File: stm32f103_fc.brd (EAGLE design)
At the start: 37.7 x 72 mm, 50 parts, among them IC1 STM32F103C8T6, IC2 LD1117AS33TR, Y1 8MHz, Y2 32.768MHz

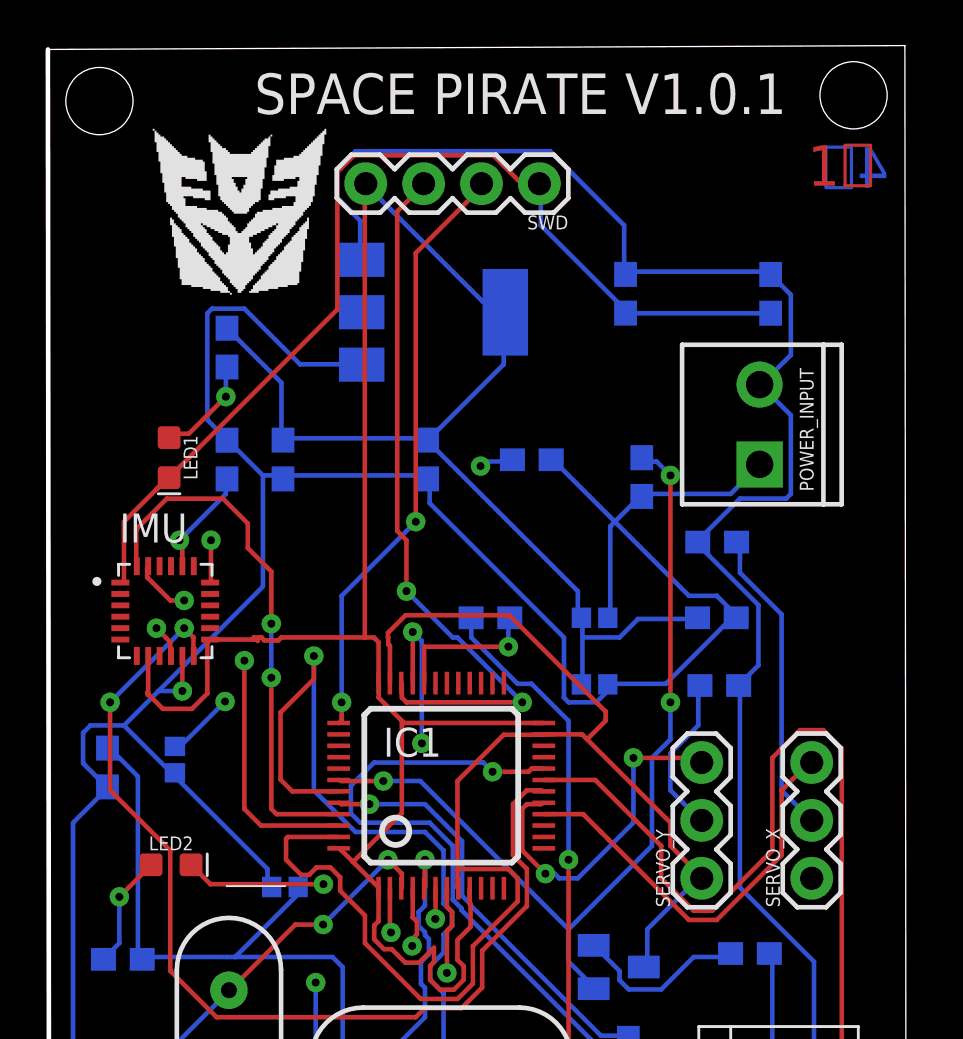
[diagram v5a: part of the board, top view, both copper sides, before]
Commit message: added serial port
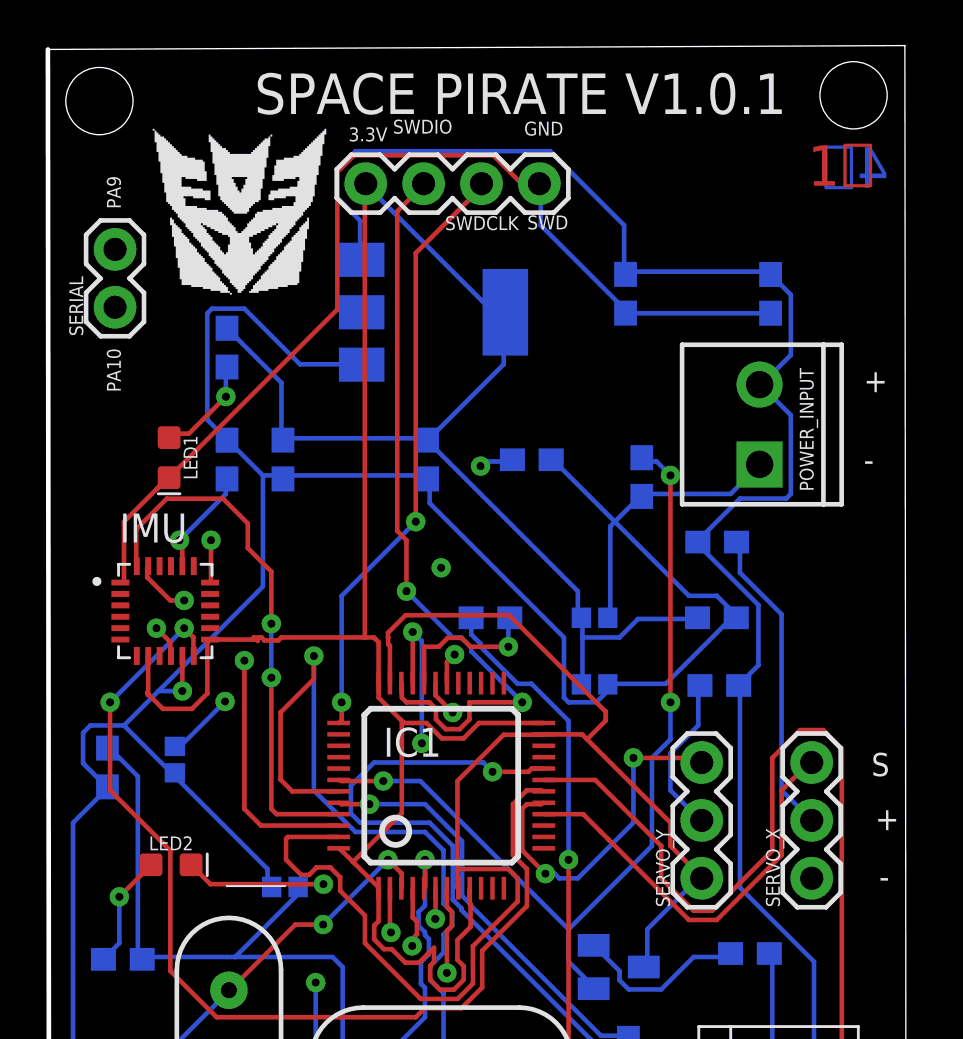
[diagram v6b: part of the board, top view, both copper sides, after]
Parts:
- added SERIAL: (no value), SparkFun-Connectors:1X02
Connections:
- net PA10: now also SERIAL.1
- net PA9: now also SERIAL.2
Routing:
- net PA9: track 0.00 -> 28.7 mm, vias 0 -> 2
- net PA10: track 0.00 -> 26.2 mm, vias 0 -> 1
- net SWDIO: track 31.6 -> 33.4 mm
- net VCC3V3: track 162.2 -> 162.8 mm
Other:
- board text added: "+"
- board text added: "-"
- board text added: "3.3V"
- board text added: "GND"
- board text added: "PA10"
- board text added: "PA9"
- board text added: "S"
- board text added: "SWDCLK"
- board text added: "SWDIO"
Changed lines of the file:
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@@
 <text x="59.68403125" y="77.12361875" size="1.778" layer="15">3层</text>
 <text x="62.816384375" y="77.0389625" size="1.778" layer="16" rot="MR0">4层</text>
+<text x="29.122421875" y="76.107721875" size="0.6096" layer="21" rot="R90">PA9</text>
+<text x="29.122421875" y="68.06519375" size="0.6096" layer="21" rot="R90">PA10</text>
+<text x="39.1120875" y="79.070759375" size="0.6096" layer="21">3.3V</text>
+<text x="46.815984375" y="79.324734375" size="0.6096" layer="21">GND</text>
+<text x="41.059228125" y="79.409390625" size="0.6096" layer="21">SWDIO</text>
+<text x="43.344996875" y="75.17648125" size="0.6096" layer="21">SWDCLK</text>
+<text x="61.715828125" y="68.06519375" size="1.016" layer="21">+</text>
+<text x="61.715828125" y="64.59420625" size="1.016" layer="21">-</text>
+<text x="62.223778125" y="48.84778125" size="1.016" layer="21">+</text>
+<text x="62.054459375" y="51.2182125" size="1.016" layer="21">S</text>
+<text x="62.39309375" y="46.308034375" size="1.016" layer="21">-</text>
 </plain>
 <attributes>
@@
 <attribute name="VALUE" x="47.154615625" y="65.86415625" size="0.6096" layer="28" font="vector" ratio="20" rot="MR180" align="top-center"/>
 </element>
+<element name="SERIAL" library="SparkFun-Connectors" library_urn="urn:adsk.eagle:library:513" package="1X02" package3d_urn="urn:adsk.eagle:package:38039/1" value="" x="28.868446875" y="71.790153125" smashed="yes" rot="R90">
+<attribute name="NAME" x="27.471446875" y="70.520153125" size="0.6096" layer="25" font="vector" ratio="20" rot="R90"/>
+<attribute name="VALUE" x="30.900446875" y="70.520153125" size="0.6096" layer="27" font="vector" ratio="20" rot="R90"/>
+</element>
 </elements>
 <signals>
@@
 <wire x1="42.69585625" y1="42.887025" x2="42.863275" y2="43.05444375" width="0.2032" layer="1"/>
 <wire x1="42.863275" y1="43.05444375" x2="42.863275" y2="43.688" width="0.2032" layer="1"/>
-<wire x1="47.68" y1="53.55" x2="41.5476" y2="53.55" width="0.2032" layer="1"/>
 <wire x1="41.5476" y1="53.55" x2="41.4528" y2="53.6448" width="0.2032" layer="1"/>
 <wire x1="34.966959375" y1="31.668125" x2="38.8581125" y2="35.559278125" width="0.2032" layer="16"/>
@@
 <wire x1="38.8581125" y1="42.83705" x2="38.4135625" y2="43.2816" width="0.2032" layer="16"/>
 <wire x1="38.4135625" y1="43.2816" x2="34.1376" y2="43.2816" width="0.2032" layer="16"/>
+<wire x1="44.15591875" y1="52.87173125" x2="43.21134375" y2="52.87173125" width="0.2032" layer="1"/>
+<wire x1="47.68" y1="53.55" x2="44.8341875" y2="53.55" width="0.2032" layer="1"/>
+<wire x1="42.533075" y1="53.55" x2="41.5476" y2="53.55" width="0.2032" layer="1"/>
+<wire x1="44.8341875" y1="53.55" x2="44.15591875" y2="52.87173125" width="0.2032" layer="1"/>
+<wire x1="43.21134375" y1="52.87173125" x2="42.533075" y2="53.55" width="0.2032" layer="1"/>
 </signal>
 <signal name="N$1">
@@
 <contactref element="MICRO-USB" pad="D-"/>
 <contactref element="R10" pad="1"/>
-<wire x1="44.5008" y1="57.3024" x2="44.5008" y2="58.1152" width="0.2032" layer="16"/>
-<wire x1="46.5328" y1="55.2704" x2="44.5008" y2="57.3024" width="0.2032" layer="16"/>
 <wire x1="47.1424" y1="55.2704" x2="46.5328" y2="55.2704" width="0.2032" layer="16"/>
 <wire x1="48.768" y1="53.6448" x2="47.1424" y2="55.2704" width="0.2032" layer="16"/>
@@
 <wire x1="35.3568" y1="17.272" x2="35.3330375" y2="17.297390625" width="0.2032" layer="1"/>
 <via x="48.768" y="47.5488" extent="1-16" drill="0.35"/>
+<wire x1="46.5328" y1="55.2704" x2="44.9085" y2="56.8947" width="0.2032" layer="16"/>
+<wire x1="44.9085" y1="56.8947" x2="44.9085" y2="57.02396875" width="0.2032" layer="16"/>
+<wire x1="44.9085" y1="57.02396875" x2="44.5008" y2="57.43166875" width="0.2032" layer="16"/>
+<wire x1="44.5008" y1="57.43166875" x2="44.5008" y2="58.1152" width="0.2032" layer="16"/>
 </signal>
 <signal name="PA11">
@@
 <contactref element="IC1" pad="32"/>
 <wire x1="46.1264" y1="56.896" x2="46.1264" y2="58.1152" width="0.2032" layer="16"/>
-<wire x1="46.1264" y1="56.896" x2="42.43" y2="56.896" width="0.2032" layer="1"/>
 <wire x1="46.1264" y1="58.1152" x2="46.189" y2="58.166" width="0.2032" layer="16"/>
 <via x="46.1264" y="56.896" extent="1-16" drill="0.35"/>
-<wire x1="42.43" y1="55.3" x2="42.43" y2="56.890309375" width="0.2032" layer="1"/>
-<wire x1="42.43" y1="56.896" x2="42.43" y2="56.890309375" width="0.2032" layer="1"/>
+<wire x1="46.1264" y1="56.896" x2="44.46173125" y2="56.896" width="0.2032" layer="1"/>
+<wire x1="44.46173125" y1="56.896" x2="44.07224375" y2="57.2854875" width="0.2032" layer="1"/>
+<wire x1="44.07224375" y1="57.2854875" x2="43.46434375" y2="57.2854875" width="0.2032" layer="1"/>
+<wire x1="43.46434375" y1="57.2854875" x2="43.07485625" y2="56.896" width="0.2032" layer="1"/>
+<wire x1="43.07485625" y1="56.896" x2="42.43" y2="56.896" width="0.2032" layer="1"/>
+<wire x1="42.43" y1="56.896" x2="42.43" y2="55.3" width="0.2032" layer="1"/>
 </signal>
 <signal name="N$8">
@@
 <wire x1="41.4528" y1="54.6608" x2="41.4528" y2="55.2704" width="0.2032" layer="1"/>
 <wire x1="41.656" y1="54.4576" x2="41.4528" y2="54.6608" width="0.2032" layer="1"/>
-<wire x1="46.736" y1="54.4576" x2="41.656" y2="54.4576" width="0.2032" layer="1"/>
-<wire x1="43.8912" y1="57.3024" x2="46.736" y2="54.4576" width="0.2032" layer="16"/>
-<wire x1="43.688" y1="57.3024" x2="43.8912" y2="57.3024" width="0.2032" layer="16"/>
 <wire x1="41.656" y1="59.3344" x2="43.688" y2="57.3024" width="0.2032" layer="16"/>
 <wire x1="41.656" y1="61.5696" x2="41.656" y2="59.3344" width="0.2032" layer="1"/>
@@
 <via x="46.736" y="54.4576" extent="1-16" drill="0.35"/>
 <via x="41.656" y="59.3344" extent="1-16" drill="0.35"/>
+<wire x1="44.5021" y1="56.85563125" x2="44.5021" y2="56.6915" width="0.2032" layer="16"/>
+<wire x1="44.5021" y1="56.6915" x2="46.736" y2="54.4576" width="0.2032" layer="16"/>
+<wire x1="43.688" y1="57.3024" x2="44.05533125" y2="57.3024" width="0.2032" layer="16"/>
+<wire x1="44.05533125" y1="57.3024" x2="44.5021" y2="56.85563125" width="0.2032" layer="16"/>
+<wire x1="44.41743125" y1="53.70798125" x2="43.98758125" y2="53.27813125" width="0.2032" layer="1"/>
+<wire x1="43.98758125" y1="53.27813125" x2="43.37968125" y2="53.27813125" width="0.2032" layer="1"/>
+<wire x1="43.37968125" y1="53.27813125" x2="42.94983125" y2="53.70798125" width="0.2032" layer="1"/>
+<wire x1="42.94983125" y1="53.70798125" x2="42.94983125" y2="54.17099375" width="0.2032" layer="1"/>
+<wire x1="42.94983125" y1="54.17099375" x2="42.663225" y2="54.4576" width="0.2032" layer="1"/>
+<wire x1="42.663225" y1="54.4576" x2="41.656" y2="54.4576" width="0.2032" layer="1"/>
+<wire x1="46.736" y1="54.4576" x2="44.41743125" y2="54.4576" width="0.2032" layer="1"/>
+<wire x1="44.41743125" y1="54.4576" x2="44.41743125" y2="53.70798125" width="0.2032" layer="1"/>
 </signal>
 <signal name="SWDCLK">
@@
 <signal name="PA10">
 <contactref element="IC1" pad="31"/>
+<contactref element="SERIAL" pad="1"/>
+<wire x1="28.868446875" y1="71.790153125" x2="29.88434375" y2="70.77425625" width="0.2032" layer="15"/>
+<wire x1="29.88434375" y1="70.77425625" x2="29.88434375" y2="67.30326875" width="0.2032" layer="15"/>
+<wire x1="29.88434375" y1="67.30326875" x2="37.75755625" y2="59.43005625" width="0.2032" layer="15"/>
+<wire x1="37.75755625" y1="58.752790625" x2="37.75755625" y2="59.43005625" width="0.2032" layer="15"/>
+<wire x1="42.93" y1="55.3" x2="42.93" y2="54.7655625" width="0.2032" layer="1"/>
+<wire x1="42.93" y1="54.7655625" x2="43.68363125" y2="54.01193125" width="0.2032" layer="1"/>
+<via x="43.68363125" y="54.01193125" extent="1-16" drill="0.35"/>
+<wire x1="43.68363125" y1="54.01193125" x2="42.498415625" y2="54.01193125" width="0.2032" layer="15"/>
+<wire x1="42.498415625" y1="54.01193125" x2="37.75755625" y2="58.752790625" width="0.2032" layer="15"/>
 </signal>
 <signal name="PA9">
 <contactref element="IC1" pad="30"/>
+<contactref element="SERIAL" pad="2"/>
+<wire x1="43.43" y1="55.3" x2="43.43" y2="56.2133875" width="0.2032" layer="1"/>
+<wire x1="43.43" y1="56.2133875" x2="43.768290625" y2="56.551678125" width="0.2032" layer="1"/>
+<via x="43.768290625" y="56.551678125" extent="1-16" drill="0.35"/>
+<wire x1="43.768290625" y1="56.551678125" x2="43.17568125" y2="57.1442875" width="0.2032" layer="2"/>
+<wire x1="43.17568125" y1="57.1442875" x2="43.17568125" y2="60.361296875" width="0.2032" layer="2"/>
+<via x="43.17568125" y="60.361296875" extent="1-16" drill="0.35"/>
+<wire x1="43.17568125" y1="60.361296875" x2="42.244440625" y2="61.2925375" width="0.2032" layer="15"/>
+<wire x1="42.244440625" y1="61.2925375" x2="37.16495" y2="61.2925375" width="0.2032" layer="15"/>
+<wire x1="37.16495" y1="61.2925375" x2="30.90024375" y2="67.55724375" width="0.2032" layer="15"/>
+<wire x1="30.90024375" y1="67.55724375" x2="30.90024375" y2="72.97536875" width="0.2032" layer="15"/>
+<wire x1="30.90024375" y1="72.97536875" x2="29.545459375" y2="74.330153125" width="0.2032" layer="15"/>
+<wire x1="29.545459375" y1="74.330153125" x2="28.868446875" y2="74.330153125" width="0.2032" layer="15"/>
 </signal>
 <signal name="PA8">
